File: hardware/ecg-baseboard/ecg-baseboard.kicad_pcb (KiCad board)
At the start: 2 copper layers, 2 parts, among them J1 Protocentral MAX30003

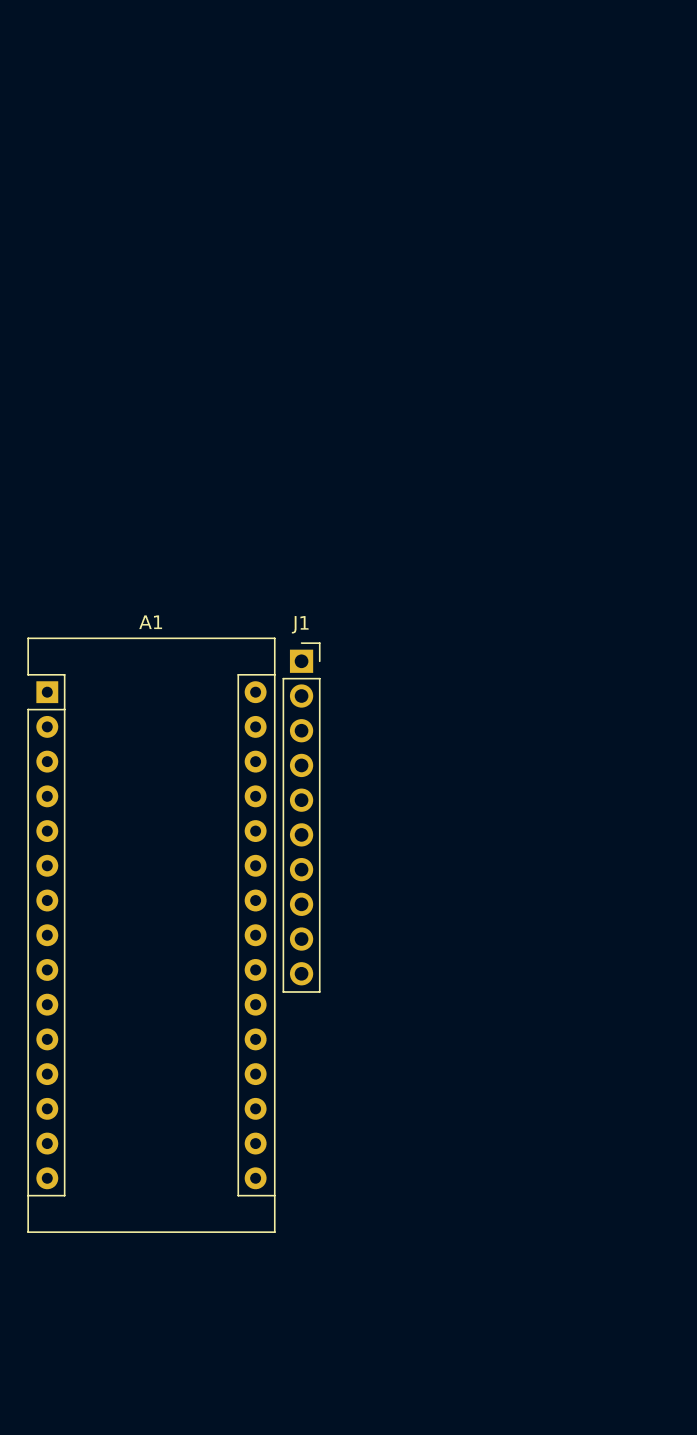
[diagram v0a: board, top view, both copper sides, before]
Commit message: Add basic pcb layout
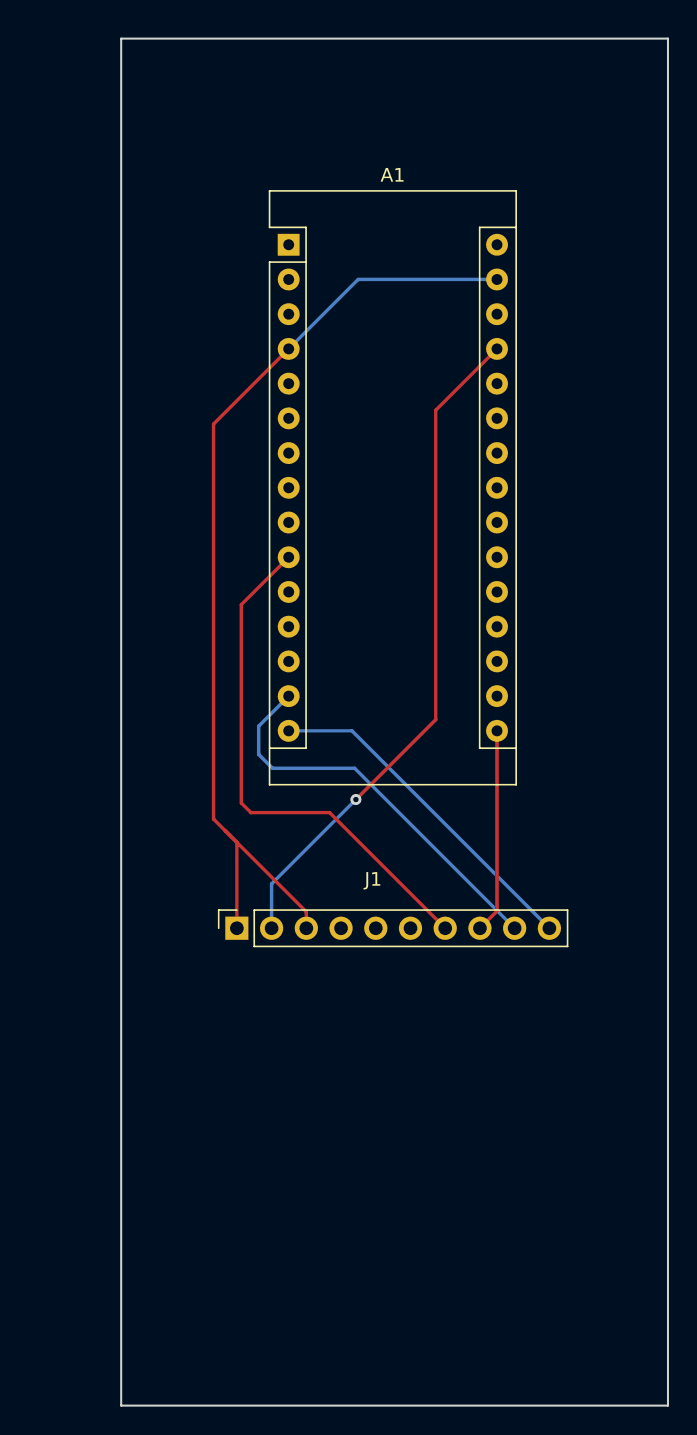
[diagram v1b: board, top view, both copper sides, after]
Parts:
- moved A1 37.2 mm to (212.3, 65.1)
- moved J1 20.1 mm to (208.5, 115.1), turned to 90 degrees
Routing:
- net GND: track 0.00 -> 72.3 mm
- net Net-(A1-Pad27): track 0.00 -> 49.2 mm, vias 0 -> 1
- net Net-(A1-Pad10): track 0.00 -> 38.1 mm
- net Net-(A1-Pad14): track 0.00 -> 29.2 mm
- net Net-(A1-Pad15): track 0.00 -> 25.1 mm, vias 0 -> 1
- net Net-(A1-Pad16): track 0.00 -> 15.0 mm
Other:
- board outline added: 40 x 100 mm
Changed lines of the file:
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@@
   (general
     (thickness 1.6)
-    (drawings 0)
-    (tracks 0)
+    (drawings 4)
+    (tracks 30)
     (zones 0)
     (modules 2)
@@
     (mod_text_size 1 1)
     (mod_text_width 0.15)
-    (pad_size 1.524 1.524)
-    (pad_drill 0.762)
+    (pad_size 1.7 1.7)
+    (pad_drill 1)
     (pad_to_mask_clearance 0.2)
     (aux_axis_origin 0 0)
@@
   )
   (module Module:Arduino_Nano (layer F.Cu)
-    (at 194.595001 97.811001)
+    (at 212.254 65.08)
     (descr "Arduino Nano, http://www.mouser.com/pdfdocs/Gravitech_Arduino_Nano3_0.pdf")
     (tags "Arduino Nano")
@@
   )
   (module Connector_PinSocket_2.54mm:PinSocket_1x10_P2.54mm_Vertical (layer F.Cu)
-    (at 213.195001 95.551001)
+    (at 208.464 115.08 90)
     (descr "Through hole straight socket strip, 1x10, 2.54mm pitch, single row (from Kicad 4.0.7), script generated")
     (tags "Through hole socket strip THT 1x10 2.54mm single row")
-    (fp_text reference J1 (at 0 -2.77) (layer F.SilkS)
-      (effects (font (size 1 1) (thickness 0.15)))
-    )
-    (fp_text value "Protocentral MAX30003" (at 0 25.63) (layer F.Fab)
+    (fp_text reference J1 (at 3.574 9.976 180) (layer F.SilkS)
+      (effects (font (size 1 1) (thickness 0.15)))
+    )
+    (fp_text value "Protocentral MAX30003" (at -3.284 10.484 180) (layer F.Fab)
       (effects (font (size 1 1) (thickness 0.15)))
     )
@@
     (fp_line (start 1.75 24.6) (end -1.8 24.6) (layer F.CrtYd) (width 0.05))
     (fp_line (start -1.8 24.6) (end -1.8 -1.8) (layer F.CrtYd) (width 0.05))
-    (fp_text user %R (at 0 11.43 90) (layer F.Fab)
-      (effects (font (size 1 1) (thickness 0.15)))
-    )
-    (pad 1 thru_hole rect (at 0 0) (size 1.7 1.7) (drill 1) (layers *.Cu *.Mask)
+    (fp_text user %R (at 0 11.43 180) (layer F.Fab)
+      (effects (font (size 1 1) (thickness 0.15)))
+    )
+    (pad 1 thru_hole rect (at 0 0 90) (size 1.7 1.7) (drill 1) (layers *.Cu *.Mask)
       (net 7 GND))
-    (pad 2 thru_hole oval (at 0 2.54) (size 1.7 1.7) (drill 1) (layers *.Cu *.Mask)
+    (pad 2 thru_hole oval (at 0 2.54 90) (size 1.7 1.7) (drill 1) (layers *.Cu *.Mask)
       (net 22 "Net-(A1-Pad27)"))
-    (pad 3 thru_hole oval (at 0 5.08) (size 1.7 1.7) (drill 1) (layers *.Cu *.Mask)
+    (pad 3 thru_hole oval (at 0 5.08 90) (size 1.7 1.7) (drill 1) (layers *.Cu *.Mask)
       (net 7 GND))
-    (pad 4 thru_hole oval (at 0 7.62) (size 1.7 1.7) (drill 1) (layers *.Cu *.Mask)
+    (pad 4 thru_hole oval (at 0 7.62 90) (size 1.7 1.7) (drill 1) (layers *.Cu *.Mask)
       (net 30 "Net-(J1-Pad4)"))
-    (pad 5 thru_hole oval (at 0 10.16) (size 1.7 1.7) (drill 1) (layers *.Cu *.Mask)
+    (pad 5 thru_hole oval (at 0 10.16 90) (size 1.7 1.7) (drill 1) (layers *.Cu *.Mask)
       (net 31 "Net-(J1-Pad5)"))
-    (pad 6 thru_hole oval (at 0 12.7) (size 1.7 1.7) (drill 1) (layers *.Cu *.Mask)
+    (pad 6 thru_hole oval (at 0 12.7 90) (size 1.7 1.7) (drill 1) (layers *.Cu *.Mask)
       (net 32 "Net-(J1-Pad6)"))
-    (pad 7 thru_hole oval (at 0 15.24) (size 1.7 1.7) (drill 1) (layers *.Cu *.Mask)
+    (pad 7 thru_hole oval (at 0 15.24 90) (size 1.7 1.7) (drill 1) (layers *.Cu *.Mask)
       (net 19 "Net-(A1-Pad10)"))
-    (pad 8 thru_hole oval (at 0 17.78) (size 1.7 1.7) (drill 1) (layers *.Cu *.Mask)
+    (pad 8 thru_hole oval (at 0 17.78 90) (size 1.7 1.7) (drill 1) (layers *.Cu *.Mask)
       (net 29 "Net-(A1-Pad16)"))
-    (pad 9 thru_hole oval (at 0 20.32) (size 1.7 1.7) (drill 1) (layers *.Cu *.Mask)
+    (pad 9 thru_hole oval (at 0 20.32 90) (size 1.7 1.7) (drill 1) (layers *.Cu *.Mask)
       (net 26 "Net-(A1-Pad14)"))
-    (pad 10 thru_hole oval (at 0 22.86) (size 1.7 1.7) (drill 1) (layers *.Cu *.Mask)
+    (pad 10 thru_hole oval (at 0 22.86 90) (size 1.7 1.7) (drill 1) (layers *.Cu *.Mask)
       (net 28 "Net-(A1-Pad15)"))
     (model ${KISYS3DMOD}/Connector_PinSocket_2.54mm.3dshapes/PinSocket_1x10_P2.54mm_Vertical.wrl
@@
     )
   )
+  (gr_line (start 200 150) (end 240 150) (layer Edge.Cuts) (width 0.15))
+  (gr_line (start 240 50) (end 240 150) (layer Edge.Cuts) (width 0.15))
+  (gr_line (start 200 50) (end 240 50) (layer Edge.Cuts) (width 0.15))
+  (gr_line (start 200 50) (end 200 150) (layer Edge.Cuts) (width 0.15))
+  (segment (start 213.544 115.08) (end 213.544 113.877919) (width 0.25) (layer F.Cu) (net 7))
+  (segment (start 206.756 78.198) (end 212.254 72.7) (width 0.25) (layer F.Cu) (net 7))
+  (segment (start 206.756 107.089919) (end 206.756 78.198) (width 0.25) (layer F.Cu) (net 7))
+  (segment (start 208.464 108.797919) (end 207.616081 107.95) (width 0.25) (layer F.Cu) (net 7))
+  (segment (start 208.464 115.08) (end 208.464 108.797919) (width 0.25) (layer F.Cu) (net 7))
+  (segment (start 207.616081 107.95) (end 206.756 107.089919) (width 0.25) (layer F.Cu) (net 7))
+  (segment (start 213.544 113.877919) (end 207.616081 107.95) (width 0.25) (layer F.Cu) (net 7))
+  (segment (start 217.334 67.62) (end 227.494 67.62) (width 0.25) (layer B.Cu) (net 7))
+  (segment (start 212.254 72.7) (end 217.334 67.62) (width 0.25) (layer B.Cu) (net 7))
+  (segment (start 209.492009 106.622009) (end 208.788 105.918) (width 0.25) (layer F.Cu) (net 19))
+  (segment (start 215.246009 106.622009) (end 209.492009 106.622009) (width 0.25) (layer F.Cu) (net 19))
+  (segment (start 223.704 115.08) (end 215.246009 106.622009) (width 0.25) (layer F.Cu) (net 19))
+  (segment (start 208.788 91.406) (end 212.254 87.94) (width 0.25) (layer F.Cu) (net 19))
+  (segment (start 208.788 105.918) (end 208.788 91.406) (width 0.25) (layer F.Cu) (net 19))
+  (segment (start 211.004 115.08) (end 211.004 111.83) (width 0.25) (layer B.Cu) (net 22))
+  (via (at 217.17 105.664) (size 0.8) (drill 0.4) (layers F.Cu B.Cu) (net 22))
+  (segment (start 211.004 111.83) (end 217.17 105.664) (width 0.25) (layer B.Cu) (net 22))
+  (segment (start 217.17 105.664) (end 223.012 99.822) (width 0.25) (layer F.Cu) (net 22))
+  (segment (start 223.012 77.182) (end 227.494 72.7) (width 0.25) (layer F.Cu) (net 22))
+  (segment (start 223.012 99.822) (end 223.012 77.182) (width 0.25) (layer F.Cu) (net 22))
+  (segment (start 228.784 115.08) (end 217.082 103.378) (width 0.25) (layer B.Cu) (net 26))
+  (segment (start 217.082 103.378) (end 211.074 103.378) (width 0.25) (layer B.Cu) (net 26))
+  (segment (start 211.074 103.378) (end 210.058 102.362) (width 0.25) (layer B.Cu) (net 26))
+  (segment (start 210.058 100.296) (end 212.254 98.1) (width 0.25) (layer B.Cu) (net 26))
+  (segment (start 210.058 102.362) (end 210.058 100.296) (width 0.25) (layer B.Cu) (net 26))
+  (via (at 212.254 100.64) (size 0.8) (drill 0.4) (layers F.Cu B.Cu) (net 28))
+  (segment (start 216.884 100.64) (end 212.254 100.64) (width 0.25) (layer B.Cu) (net 28))
+  (segment (start 231.324 115.08) (end 216.884 100.64) (width 0.25) (layer B.Cu) (net 28))
+  (segment (start 227.494 113.83) (end 227.494 100.64) (width 0.25) (layer F.Cu) (net 29))
+  (segment (start 226.244 115.08) (end 227.494 113.83) (width 0.25) (layer F.Cu) (net 29))
 )

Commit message: Add silkscren text, logo, gnd copper fill, traces
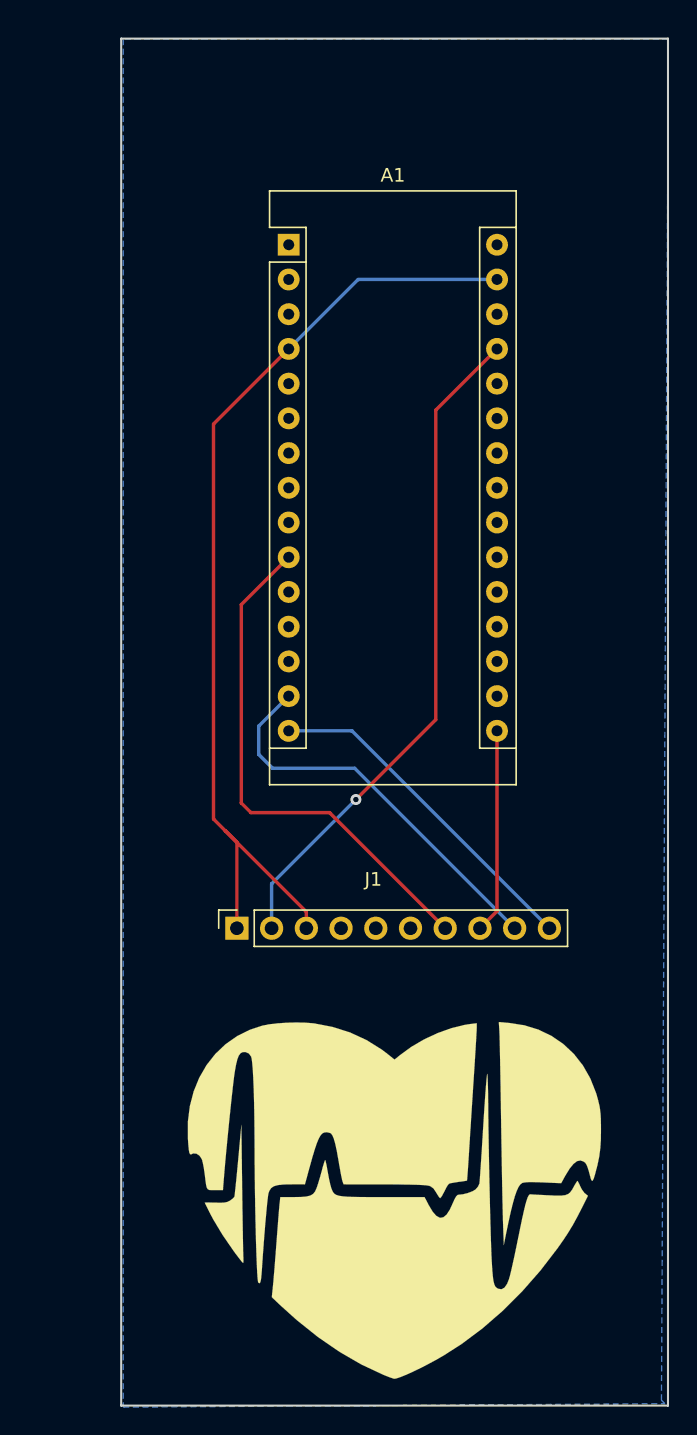
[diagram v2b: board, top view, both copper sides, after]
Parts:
- added G***: LOGO, ecg-baseboard:heart-logo, F.Cu at (220.0, 135.0)
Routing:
- added copper zone on B.Cu, net GND
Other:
- board text added: "ECG Baseboard araBeat v0.1"

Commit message: Add edgecut, mounting hole and component aligments
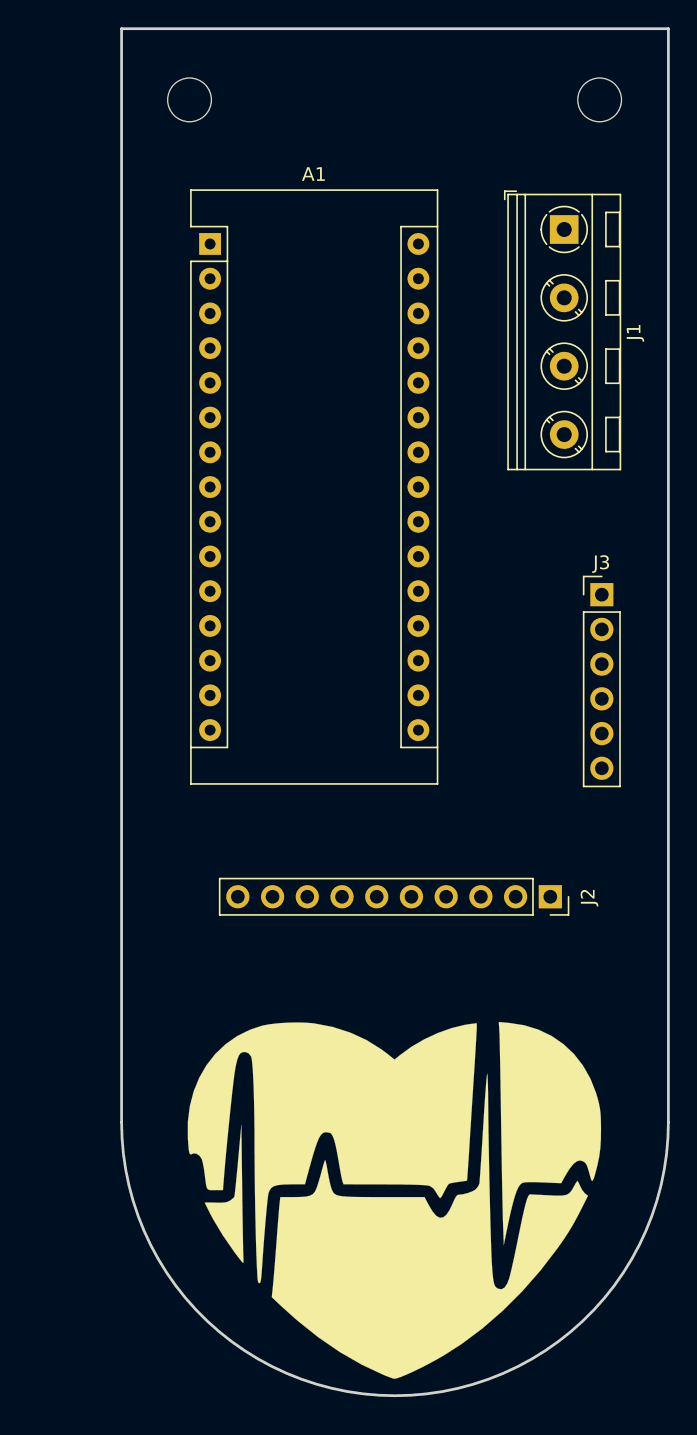
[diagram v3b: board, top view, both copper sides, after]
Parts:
- added ?: MountingHole_3.2mm_M3, MountingHole:MountingHole_3.2mm_M3, F.Cu at (205.0, 54.5)
- added ?: MountingHole_3.2mm_M3, MountingHole:MountingHole_3.2mm_M3, F.Cu at (235.0, 54.5)
- added J2: Protocentral MAX30003, Connector_PinSocket_2.54mm:PinSocket_1x10_P2.54mm_Vertical, F.Cu at (231.4, 112.8)
- added J3: Conn_01x06, Connector_PinHeader_2.54mm:PinHeader_1x06_P2.54mm_Vertical, F.Cu at (235.2, 90.7)
- J1: value Protocentral MAX30003 -> Screw_Terminal_01x04; footprint Connector_PinSocket_2.54mm:PinSocket_1x10_P2.54mm_Vertical -> TerminalBlock_RND:TerminalBlock_RND_205-00047_1x04_P5.00mm_Horizontal
- moved J1 56.4 mm to (232.4, 64.0), turned to 270 degrees
- moved A1 5.75 mm to (206.5, 65.0)
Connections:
- A1 pad 11: Net-(A1-Pad11) -> (no net)
- A1 pad 12: Net-(A1-Pad12) -> (no net)
- A1 pad 13: Net-(A1-Pad13) -> (no net)
- A1 pad 17: Net-(A1-Pad17) -> (no net)
- A1 pad 18: Net-(A1-Pad18) -> (no net)
- A1 pad 21: Net-(A1-Pad21) -> (no net)
- A1 pad 22: Net-(A1-Pad22) -> (no net)
- A1 pad 23: Net-(A1-Pad23) -> (no net)
- A1 pad 24: Net-(A1-Pad24) -> (no net)
- A1 pad 25: Net-(A1-Pad25) -> (no net)
- A1 pad 26: Net-(A1-Pad26) -> (no net)
- A1 pad 28: Net-(A1-Pad28) -> (no net)
- A1 pad 3: Net-(A1-Pad3) -> (no net)
- A1 pad 30: Net-(A1-Pad30) -> (no net)
- A1 pad 7: Net-(A1-Pad7) -> (no net)
- A1 pad 8: Net-(A1-Pad8) -> (no net)
- A1 pad 9: Net-(A1-Pad9) -> (no net)
- J1 pad 3: GND -> Net-(A1-Pad5)
- J1 pad 4: Net-(J1-Pad4) -> Net-(A1-Pad19)
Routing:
- net GND: track 72.3 -> 0.00 mm
- net Net-(A1-Pad27): track 49.2 -> 0.00 mm, vias 1 -> 0
- net Net-(A1-Pad10): track 38.1 -> 0.00 mm
- net Net-(A1-Pad14): track 29.2 -> 0.00 mm
- net Net-(A1-Pad15): track 25.1 -> 0.00 mm, vias 1 -> 0
- net Net-(A1-Pad16): track 15.0 -> 0.00 mm
- removed copper zone on B.Cu, net GND
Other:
- outline, holes or cut-outs redrawn
- board text removed: "ECG Baseboard araBeat v0.1"

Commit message: Add complete routing, copper fill, silkscreen texts, fiducials
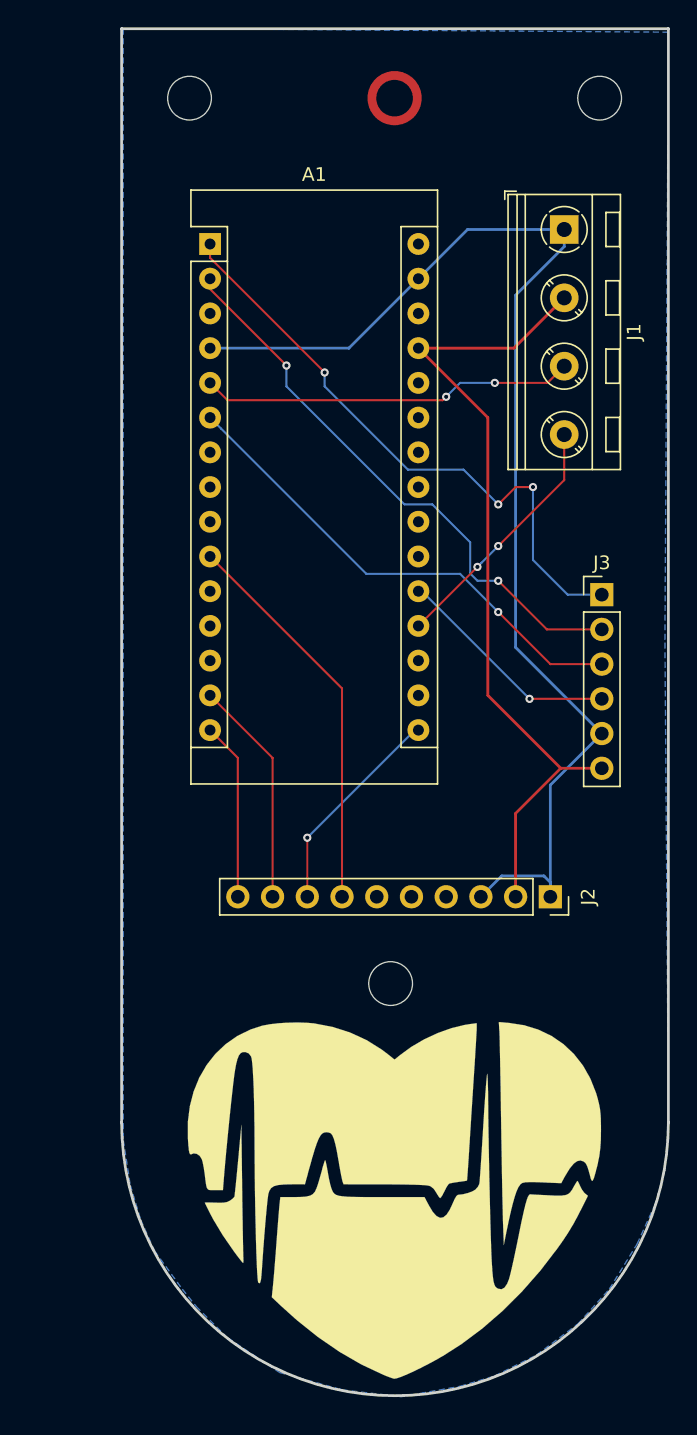
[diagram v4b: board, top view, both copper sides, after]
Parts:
- added ?: M3, MountingHole:MountingHole_3.2mm_M3, F.Cu at (219.7, 119.1)
- added ?: Fiducial_Modern_CopperTop, Fiducial:Fiducial_Modern_CopperTop, F.Cu at (220.0, 54.4)
- ? (x2): value MountingHole_3.2mm_M3 -> M3
- moved ? 0.13 mm to (205.0, 54.4)
- moved ? 0.13 mm to (235.0, 54.4)
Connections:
- net Net-(A1-Pad27) renamed /VCC
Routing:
- net GND: track 0.00 -> 90.9 mm
- net /VCC: track 0.00 -> 61.0 mm
- net Net-(A1-Pad1): track 0.00 -> 44.7 mm, vias 0 -> 3
- net Net-(A1-Pad2): track 0.00 -> 42.0 mm, vias 0 -> 2
- net Net-(A1-Pad6): track 0.00 -> 36.1 mm, vias 0 -> 1
- net Net-(A1-Pad10): track 0.00 -> 28.9 mm
- net Net-(A1-Pad5): track 0.00 -> 27.5 mm, vias 0 -> 2
- net Net-(A1-Pad19): track 0.00 -> 18.4 mm, vias 0 -> 2
- net Net-(A1-Pad20): track 0.00 -> 16.7 mm, vias 0 -> 1
- net Net-(A1-Pad14): track 0.00 -> 16.6 mm
- net Net-(A1-Pad16): track 0.00 -> 15.7 mm, vias 0 -> 1
- net Net-(A1-Pad15): track 0.00 -> 13.0 mm
- added copper zone on B.Cu, net GND
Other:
- net class PWR added: clearance 0.2032, trace_width 0.2032, via_dia 0.6, via_drill 0.3
- net class SIGNAL added: clearance 0.1524, trace_width 0.1524, via_dia 0.6, via_drill 0.3
- rule trace_min: 0.2 -> 0.1524
- rule via_min_size: 0.4 -> 0.6
- board text added: "A0"
- board text added: "A1"
- board text added: "D2"
- board text added: "D3"
- board text added: "ECG Baseboard v0.1 araBeat www.aravinth.info"
- board text added: "GND"
- board text added: "RX"
- board text added: "TX"
- board text added: "VCC"
